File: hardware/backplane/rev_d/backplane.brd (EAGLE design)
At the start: 254 x 381 mm, 386 parts, among them J0 BACKPLANE_GENERIC_MODULE, J1 BACKPLANE_GENERIC_MODULE, J2 BACKPLANE_GENERIC_MODULE, J3 BACKPLANE_CONTROLLER_MODULE, J4 BACKPLANE_POWER_MODULE, J5 BACKPLANE_GENERIC_MODULE, J6 BACKPLANE_GENERIC_MODULE, J7 BACKPLANE_GENERIC_MODULE, J8 SCREW-TERMINAL_2_0.100, J9 SCREW-TERMINAL_2_0.100, U1 TUSB2077A, U10 SN74LVC2T45, U11 SN74LVC2T45, U12 SN74LVC2T45, U13 SN74LVC2T45, U14 SN74LVC2T45, U15 SN74LVC2T45, U16 SN74LVC2T45, U17 SN74LVC2T45, U18 SN74LVC2T45, U19 SN74LVC2T45, U2 FXMA2102, U20 TS3USB30E, U21 TS3USB30E, U22 TS3USB30E, U23 TS3USB30E, U24 TS3USB30E, U25 TS3USB30E, U26 MCP23008QFN, U27 MCP23008QFN, U28 MCP23008QFN, U29 MCP23008QFN, U3 FXMA2102, U30 MCP23008QFN, U31 MCP23008QFN, U32 MCP23008QFN, U33 NCP301LSN30, U34 M24C01WMN, U4 FXMA2102, U5 FXMA2102, U6 FXMA2102, U7 FXMA2102, U8 SN74LVC2T45, U9 SN74LVC2T45, Y1 ABMM

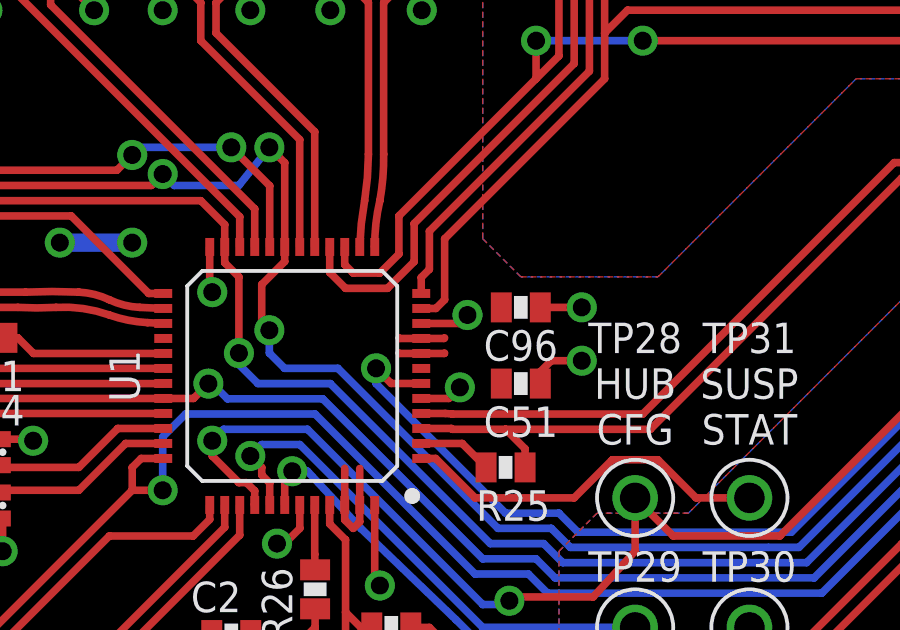
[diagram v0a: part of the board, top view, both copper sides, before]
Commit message: backplane: hub !BUSPWR -> high
Resolves errata from revC:

USB !BUSPWR is wrong: Currently tied to GND, which states that the hub and
all downstream devices are powered from the upstream port. Should be tied
high, stating that the hub has an "external" power supply. In both modes,
the hub still will perform overcurrent and poweroff protections.

  - Symptom: This limits the hub to 500mA max total draw, as each
    downstream port has a minimum 100mA allotment (USB spec), so the hub
    disables higher ports (cannot use USB in Module 5 or Module 7 slot)
  - Remedy: Cut trace at pin 10 (!BUSPWR) and short pins 10 and 9.
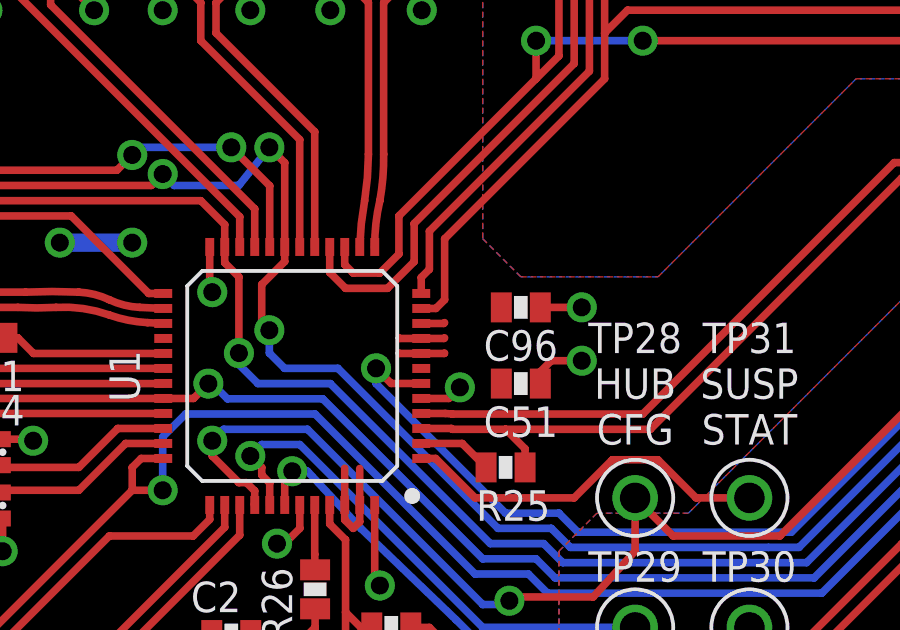
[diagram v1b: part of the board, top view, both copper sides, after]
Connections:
- net GND: no longer U1.10
- net VCC_BACKPLANE: now also U1.10
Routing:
- net GND: track 3335.8 -> 3334.1 mm, vias 264 -> 263
- net VCC_BACKPLANE: track 518.1 -> 518.9 mm
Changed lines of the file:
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@@
 <?xml version="1.0" encoding="utf-8"?>
 <!DOCTYPE eagle SYSTEM "eagle.dtd">
-<eagle version="8.1.1">
+<eagle version="8.2.2">
 <drawing>
 <settings>
@@
 <setting verticaltext="up"/>
 </settings>
-<grid distance="10" unitdist="mil" unit="mil" style="lines" multiple="1" display="yes" altdistance="0.01" altunitdist="inch" altunit="inch"/>
+<grid distance="10" unitdist="mil" unit="mil" style="lines" multiple="1" display="yes" altdistance="10" altunitdist="mil" altunit="mil"/>
 <layers>
 <layer number="1" name="Top" color="4" fill="1" visible="yes" active="yes"/>
@@
 <contactref element="R57" pad="1"/>
 <contactref element="R58" pad="1"/>
-<contactref element="U1" pad="10"/>
 <contactref element="U1" pad="5"/>
 <contactref element="U1" pad="24"/>
@@
 <wire x1="120.378" y1="189.75" x2="121.297" y2="189.75" width="0.254" layer="1"/>
 <wire x1="121.297" y1="189.75" x2="121.666" y2="190.119" width="0.254" layer="1"/>
-<wire x1="120.378" y1="192.25" x2="121.638" y2="192.25" width="0.254" layer="1"/>
-<wire x1="121.638" y1="192.25" x2="121.92" y2="192.532" width="0.254" layer="1"/>
-<via x="121.92" y="192.532" extent="1-16" drill="0.6"/>
 <wire x1="143.518" y1="188.854" x2="143.518" y2="186.586" width="0.254" layer="1"/>
 <wire x1="143.518" y1="186.586" x2="143.114" y2="186.182" width="0.254" layer="1"/>
@@
 <wire x1="145.796" y1="283.718" x2="150.1648" y2="283.718" width="0.254" layer="1"/>
 <wire x1="150.1648" y1="283.718" x2="150.2918" y2="283.845" width="0.254" layer="1"/>
+<contactref element="U1" pad="10"/>
+<wire x1="120.378" y1="192.25" x2="121.13" y2="192.25" width="0.254" layer="1"/>
+<wire x1="121.13" y1="192.25" x2="121.158" y2="192.278" width="0.254" layer="1"/>
 </signal>
 <signal name="USB_SUSPEND_STATUS">
